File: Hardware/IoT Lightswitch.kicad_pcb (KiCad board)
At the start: 2 copper layers, 39.1 x 71.1 mm, 22 parts, among them J1 Screw_Terminal_01x04, K1 SANYOU_SRD_Form_C, Q1 NMOS, SW5 SW_SPST, U1 ESP32-S2-SOLO-2

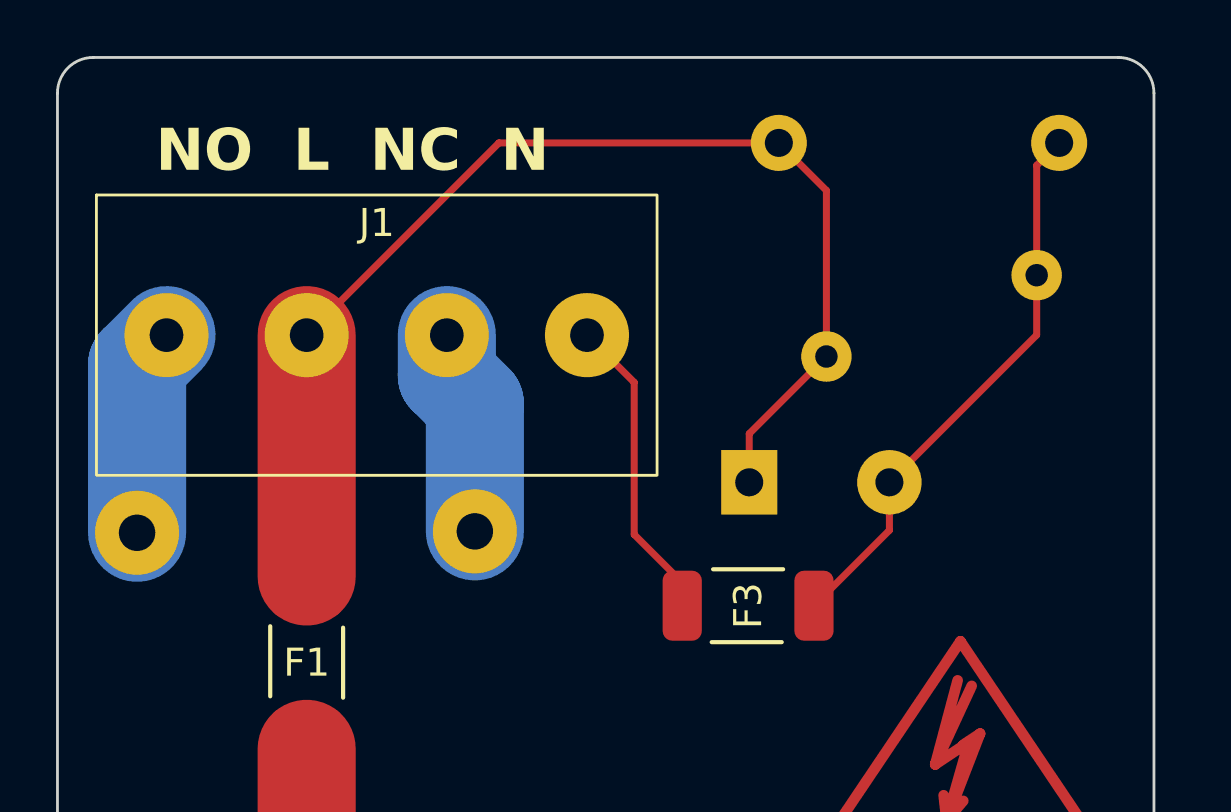
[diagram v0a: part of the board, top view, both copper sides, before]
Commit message: Moved PSU Fuse from Neutral to Live
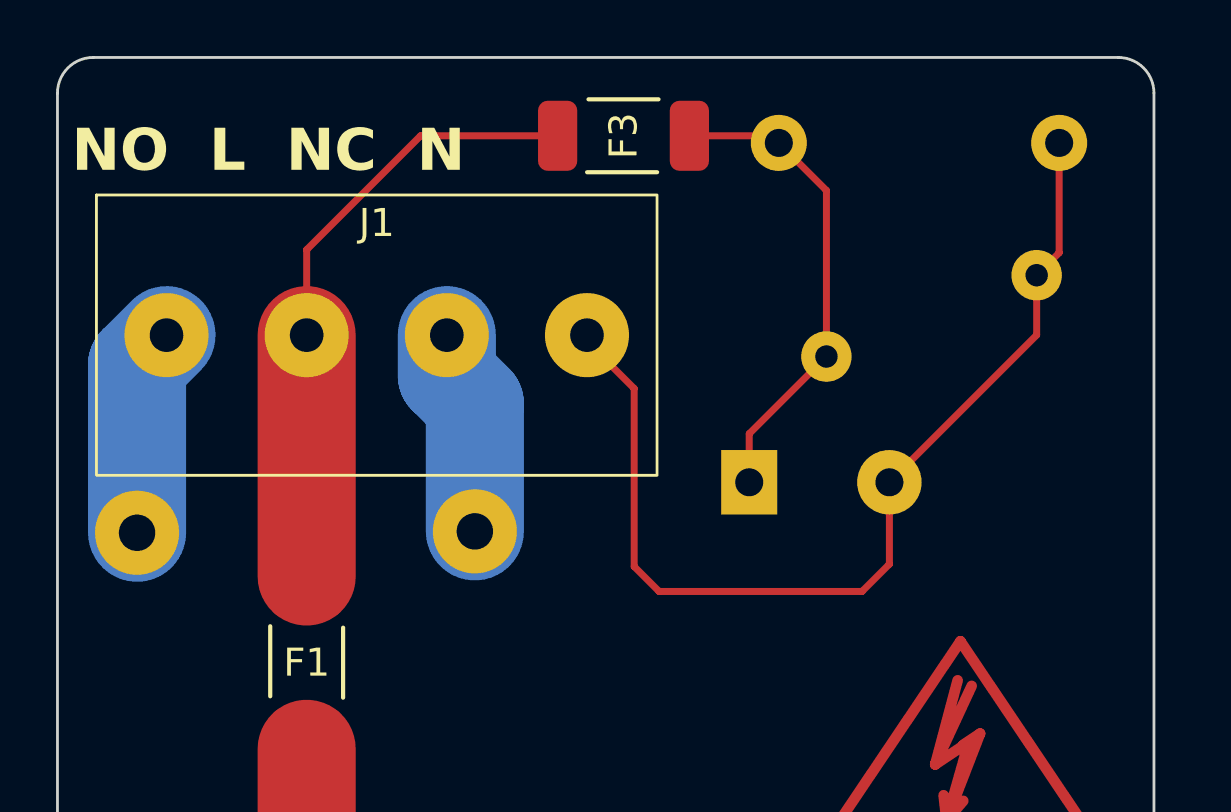
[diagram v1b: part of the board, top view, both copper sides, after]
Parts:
- F1: value Fuse -> 5A 250v
- F3: value Fuse -> 0.5A 125v
- R2: value R -> 10k
- R3: value R_Small -> 10k
- moved F3 17.3 mm to (158.9, 53.8)
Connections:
- C2 pad 1: AC_L -> Net-(PS1-AC/L)
- C2 pad 2: AC_N_FUSED -> AC_N
- F3 pad 1: AC_N -> AC_L
- F3 pad 2: AC_N_FUSED -> Net-(PS1-AC/L)
- PS1 pad 1: AC_L -> Net-(PS1-AC/L)
- PS1 pad 2: AC_N_FUSED -> AC_N
- RV1 pad 1: AC_L -> Net-(PS1-AC/L)
- RV1 pad 2: AC_N_FUSED -> AC_N
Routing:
- net AC_N: track 11.1 -> 36.4 mm
- net AC_N_FUSED: track 20.1 -> 0.00 mm
- net AC_L: track 42.2 -> 22.3 mm
- net Net-(PS1-AC/L): track 0.00 -> 17.2 mm

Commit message: Added Humidity and Temperature Sensor
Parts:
- added C4: 100n, Capacitor_SMD:C_0402_1005Metric, B.Cu at (169.3, 103.6)
- added U2: SHTC3, Sensor_Humidity:Sensirion_DFN-4-1EP_2x2mm_P1mm_EP0.7x1.6mm, B.Cu at (171.8, 103.6)
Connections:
- U1 pad 24: unconnected-(U1-IO33-Pad24) -> SDA
- U1 pad 25: unconnected-(U1-IO34-Pad25) -> SCL
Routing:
- net +3V3: track 83.3 -> 87.9 mm
- net SDA: track 0.00 -> 3.58 mm, vias 0 -> 1
- net SCL: track 0.00 -> 3.34 mm, vias 0 -> 1
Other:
- board text added: "JLCJLCJLCJLC"
- board text added: "L"
- board text added: "N"
- board text added: "NC"
- board text added: "NO"
- board text removed: "NO L NC N"
